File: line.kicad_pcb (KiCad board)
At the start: 2 copper layers, 68 parts, among them P1 CONN_01X08, P2 CONN_01X08, P3 CONN_01X03, P4 CONN_01X03, U1 TL072, U2 LM7805CT, U3 LM7905CT, U4 TL072

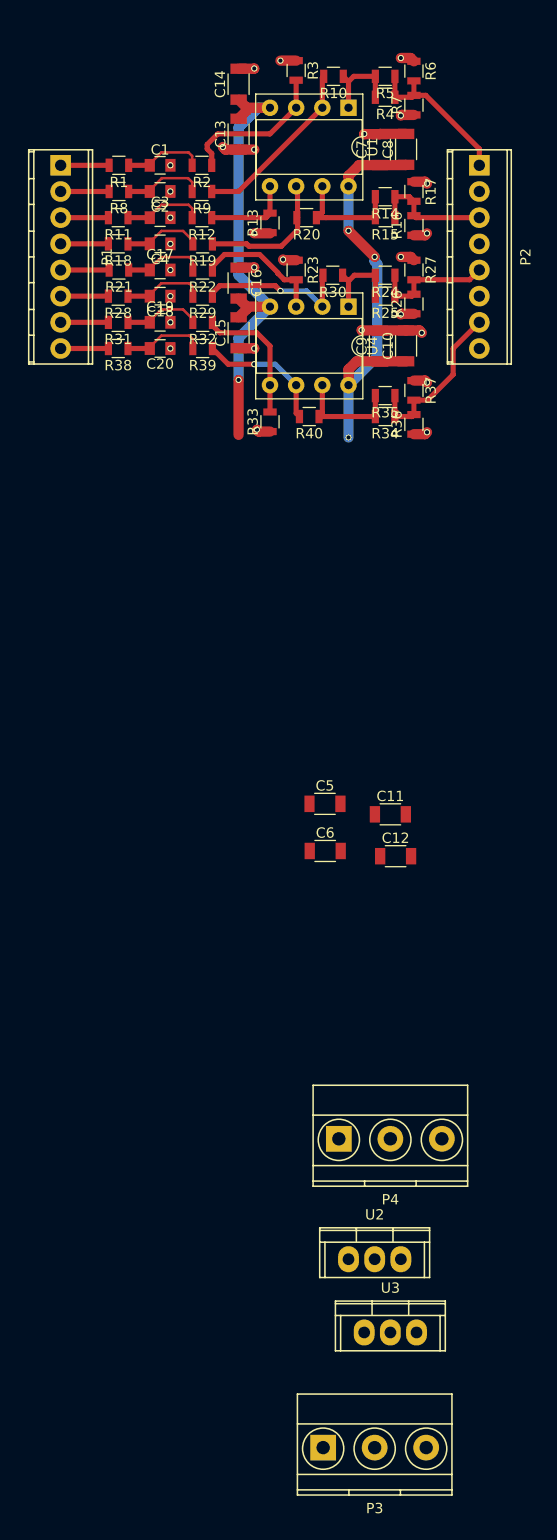
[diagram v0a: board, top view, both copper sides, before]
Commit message: added regulator layout
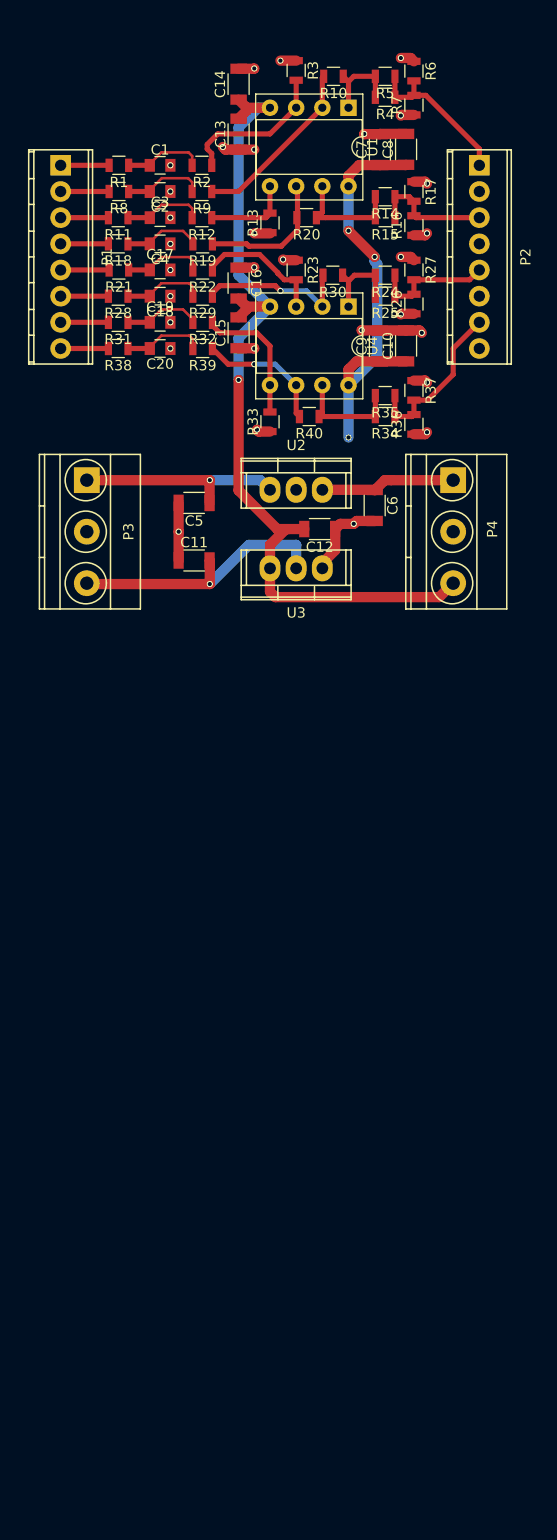
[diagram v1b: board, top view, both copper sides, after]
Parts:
- moved P3 96.7 mm to (63.5, 71.2), turned to 270 degrees
- moved U2 75.1 mm to (83.8, 72.1)
- moved U3 74.7 mm to (83.8, 79.8), turned to 180 degrees
- moved P4 64.9 mm to (99.1, 71.2), turned to 270 degrees
- moved C6 33.9 mm to (91.4, 73.7), turned to 270 degrees
- moved C12 32.6 mm to (86.1, 75.9), turned to 180 degrees
- moved C5 31.9 mm to (73.9, 73.4), turned to 180 degrees
- moved C11 31.1 mm to (73.9, 79.0)
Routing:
- net /VEE: track 45.7 -> 85.1 mm
- net Net-(C11-Pad2): track 0.00 -> 27.3 mm, vias 0 -> 1
- net Net-(C5-Pad1): track 0.00 -> 20.6 mm, vias 0 -> 1
- net GND: track 34.3 -> 48.3 mm, vias 28 -> 30
- net /VCC: track 41.2 -> 54.3 mm

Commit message: line receiver PCB looks complete
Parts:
- added FID1: FIDUCIAL, smd:FID0.5, F.Cu at (74.9, 36.8)
- added FID2: FIDUCIAL, smd:FID0.5, F.Cu at (97.8, 40.6)
- added FID3: FIDUCIAL, smd:FID0.5, F.Cu at (66.0, 78.7)
- added FID4: FIDUCIAL, smd:FID0.5, F.Cu at (101.6, 78.7)
- added REF**: hole3mm, pcb:hole3mm, F.Cu at (100.3, 88.9)
- added REF**: hole3mm, pcb:hole3mm, F.Cu at (62.2, 88.9)
- added REF**: hole3mm, pcb:hole3mm, F.Cu at (62.2, 31.8)
- added REF**: hole3mm, pcb:hole3mm, F.Cu at (100.3, 31.8)
- added REF***: OSHW-Logo2_7.3x6mm_Copper, Symbols:OSHW-Logo2_7.3x6mm_Copper, F.Cu at (67.8, 64.3)
- added REF***: OSHW-Logo2_7.3x6mm_SilkScreen, Symbols:OSHW-Logo2_7.3x6mm_SilkScreen, F.Cu at (67.8, 64.3)
- moved C12 5.33 mm to (80.8, 75.9)
- moved C6 5.11 mm to (86.9, 75.9), turned to 180 degrees
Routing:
- net /VCC: track 54.3 -> 65.1 mm
- net GND: track 48.3 -> 54.1 mm
- net /VEE: track 85.1 -> 82.5 mm
- net Net-(R32-Pad1): track 13.1 -> 13.8 mm
- added copper zone on B.Cu, net GND
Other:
- board outline added: 48.3 x 67.3 mm
- board text added: "+32"
- board text added: "-32"
- board text added: "4ch Differential Line RX"
- board text added: "A"
- board text added: "A+"
- board text added: "A-"
- board text added: "B"
- board text added: "B+"
- board text added: "B-"
- board text added: "C"
- board text added: "C+"
- board text added: "C-"
- board text added: "D"
- board text added: "D+"
- board text added: "D-"
- board text added: "GND"
- board text added: "IN"
- board text added: "Inputs"
- board text added: "OUT"
- board text added: "Outputs"
- board text added: "Rev.A 201710"
- board text added: "VCC"
- board text added: "VEE"
- board text added: "github.com/phenidone"
- board text added: "william@brodie-tyrrell.org"

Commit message: rounded corners, added gerbers
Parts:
- removed the REF*** at (67.8, 64.3)
- moved FID4 14.0 mm to (102.9, 64.8)
- moved FID1 7.62 mm to (67.3, 36.8)
- moved FID2 6.35 mm to (102.9, 36.8)
- moved FID3 1.27 mm to (67.3, 78.7)
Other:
- outline, holes or cut-outs redrawn

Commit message: converted power regulators to LM317/337 for higher voltage support
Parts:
- added R41: 510, Resistors_SMD:R_0805, F.Cu at (83.1, 69.1)
- added R42: 4k3, Resistors_SMD:R_0805, F.Cu at (86.6, 69.1)
- added R43: 4k3, Resistors_SMD:R_0805, F.Cu at (87.1, 82.8)
- added R44: 510, Resistors_SMD:R_0805, F.Cu at (81.0, 82.8)
- U2: value LM7805CT -> LM317AT
- U3: value LM7905CT -> LM337T
- moved FID4 14.0 mm to (102.9, 78.7)
- moved C12 10.2 mm to (90.2, 80.0), turned to 90 degrees
- moved FID1 7.62 mm to (59.7, 36.8)
- moved C6 5.25 mm to (90.2, 71.9), turned to 270 degrees
- moved U2 1.28 mm to (82.5, 72.3), turned to 180 degrees
- moved U3 1.27 mm to (82.5, 79.8), turned to 0 degrees
- moved R33 1.02 mm to (80.3, 65.5)
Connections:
- U2 pad 1: Net-(C5-Pad1) -> Net-(R41-Pad1)
- U2 pad 2: GND -> /VCC
- U2 pad 3: /VCC -> Net-(C5-Pad1)
- U3 pad 1: GND -> Net-(R43-Pad1)
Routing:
- net Net-(R43-Pad1): track 0.00 -> 11.8 mm
- net Net-(R41-Pad1): track 0.00 -> 5.07 mm
- net /VEE: track 82.5 -> 85.5 mm
- net Net-(C11-Pad2): track 27.3 -> 24.5 mm, vias 1 -> 0
- net GND: track 54.1 -> 51.5 mm, vias 30 -> 31
- net /VCC: track 65.1 -> 67.1 mm

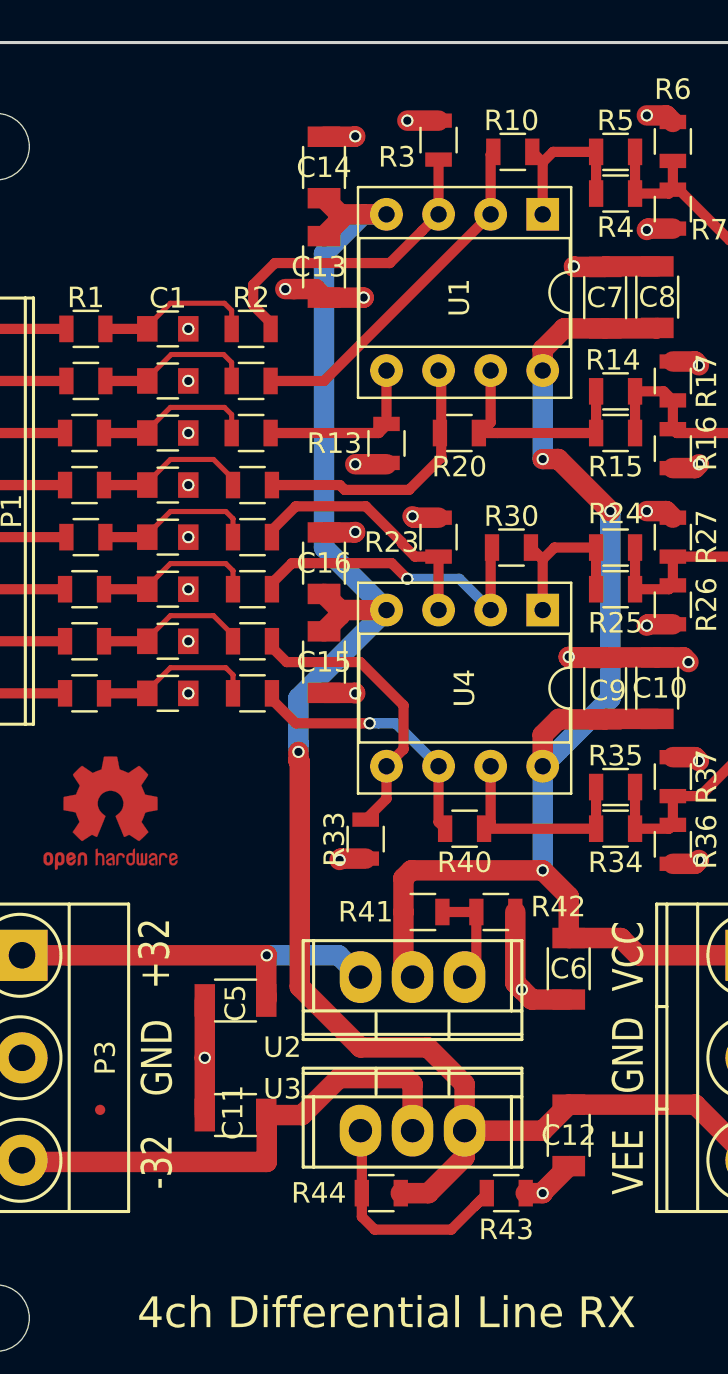
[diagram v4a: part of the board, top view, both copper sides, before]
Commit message: cleaned up silkscreen
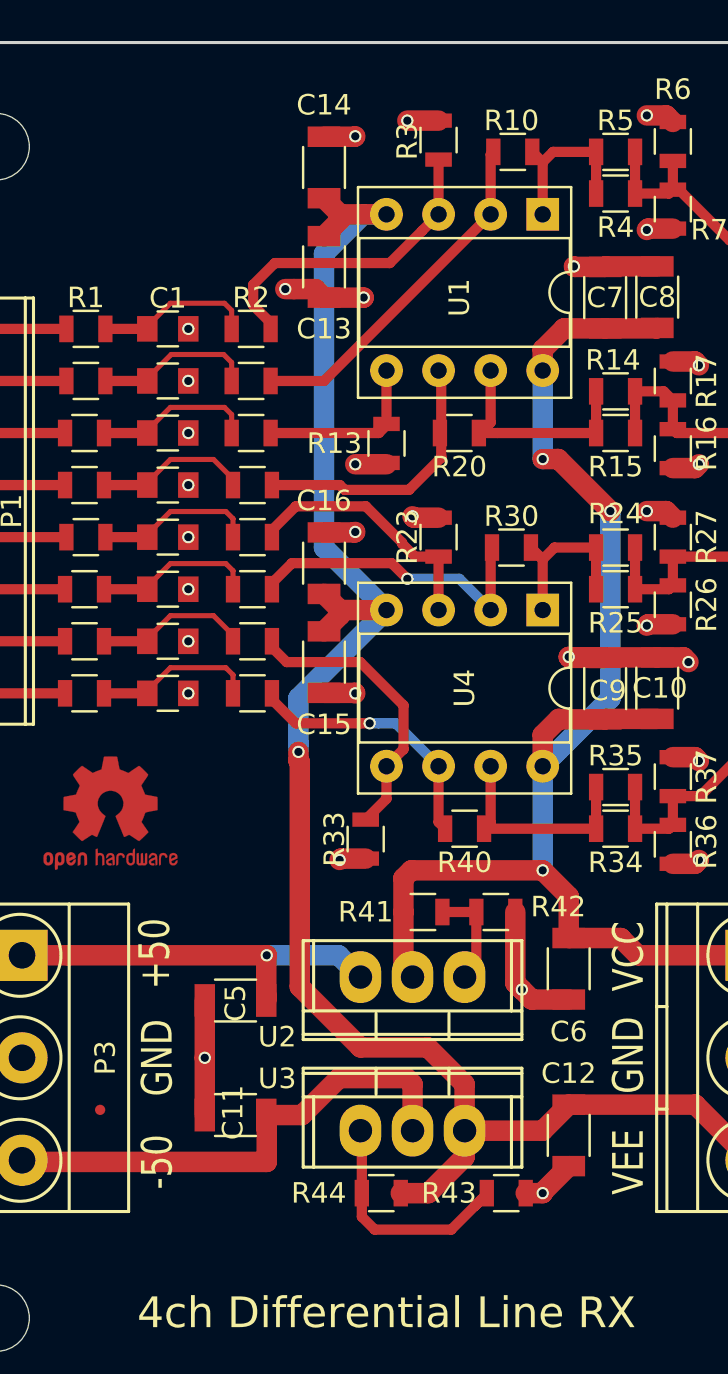
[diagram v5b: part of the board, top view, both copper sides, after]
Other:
- board text added: "+50"
- board text added: "-50"
- board text removed: "+32"
- board text removed: "-32"
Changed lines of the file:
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@@
     (tags "capacitor 1206")
     (attr smd)
-    (fp_text reference C6 (at 0 0 360) (layer F.SilkS)
+    (fp_text reference C6 (at 3.072 0 360) (layer F.SilkS)
       (effects (font (size 1 1) (thickness 0.15)))
     )
@@
     (tags "capacitor 1206")
     (attr smd)
-    (fp_text reference C12 (at 0 0 180) (layer F.SilkS)
+    (fp_text reference C12 (at 3.024 0 180) (layer F.SilkS)
       (effects (font (size 1 1) (thickness 0.15)))
     )
@@
     (tags "capacitor 1206")
     (attr smd)
-    (fp_text reference C14 (at 0 0 360) (layer F.SilkS)
+    (fp_text reference C14 (at -3.048 0 360) (layer F.SilkS)
       (effects (font (size 1 1) (thickness 0.15)))
     )
@@
     (tags "capacitor 1206")
     (attr smd)
-    (fp_text reference C16 (at 0 0 360) (layer F.SilkS)
+    (fp_text reference C16 (at -3.048 0 360) (layer F.SilkS)
       (effects (font (size 1 1) (thickness 0.15)))
     )
@@
     (tags "resistor 0805")
     (attr smd)
-    (fp_text reference R3 (at 0.828 2.032 360) (layer F.SilkS)
+    (fp_text reference R3 (at 0.066 1.524 450) (layer F.SilkS)
       (effects (font (size 1 1) (thickness 0.15)))
     )
@@
     (tags "resistor 0805")
     (attr smd)
-    (fp_text reference R23 (at 0.254 2.286 360) (layer F.SilkS)
+    (fp_text reference R23 (at 0 1.524 450) (layer F.SilkS)
       (effects (font (size 1 1) (thickness 0.15)))
     )
@@
     (tags "capacitor 1206")
     (attr smd)
-    (fp_text reference C13 (at 0 -0.254 180) (layer F.SilkS)
+    (fp_text reference C13 (at -3.024 0 180) (layer F.SilkS)
       (effects (font (size 1 1) (thickness 0.15)))
     )
@@
     (tags "capacitor 1206")
     (attr smd)
-    (fp_text reference C15 (at 0 0 180) (layer F.SilkS)
+    (fp_text reference C15 (at -3.048 0 180) (layer F.SilkS)
       (effects (font (size 1 1) (thickness 0.15)))
     )
@@
     (tags "resistor 0805")
     (attr smd)
-    (fp_text reference R43 (at 0 1.778) (layer F.SilkS)
+    (fp_text reference R43 (at -2.794 0) (layer F.SilkS)
       (effects (font (size 1 1) (thickness 0.15)))
     )
@@
     (descr "Non Isolated JEDEC TO-220 Package")
     (tags "Power Integration YN Package")
-    (fp_text reference U2 (at 6.35 -3.429 180) (layer F.SilkS)
+    (fp_text reference U2 (at 6.604 -2.921 180) (layer F.SilkS)
       (effects (font (size 1 1) (thickness 0.15)))
     )
@@
     (descr "Non Isolated JEDEC TO-220 Package")
     (tags "Power Integration YN Package")
-    (fp_text reference U3 (at -6.35 -2.032) (layer F.SilkS)
+    (fp_text reference U3 (at -6.604 -2.54) (layer F.SilkS)
       (effects (font (size 1 1) (thickness 0.15)))
     )
@@
     (effects (font (size 1.5 1.2) (thickness 0.3)))
   )
-  (gr_text -32 (at 70.104 81.28 90) (layer F.SilkS)
+  (gr_text -50 (at 70.104 81.28 90) (layer F.SilkS)
     (effects (font (size 1.5 1.2) (thickness 0.3)))
   )
-  (gr_text +32 (at 69.977 71.12 90) (layer F.SilkS)
+  (gr_text +50 (at 69.977 71.12 90) (layer F.SilkS)
     (effects (font (size 1.5 1.2) (thickness 0.3)))
   )
